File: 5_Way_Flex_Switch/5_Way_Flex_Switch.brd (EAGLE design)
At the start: 51 x 26.5 mm, 9 parts

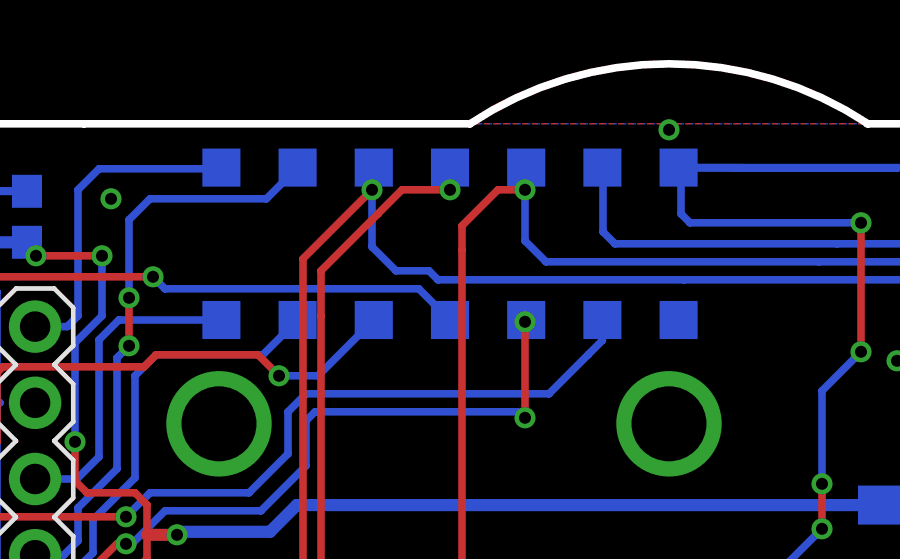
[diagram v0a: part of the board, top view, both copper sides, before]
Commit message: Updates/ label modifications to make them consistent
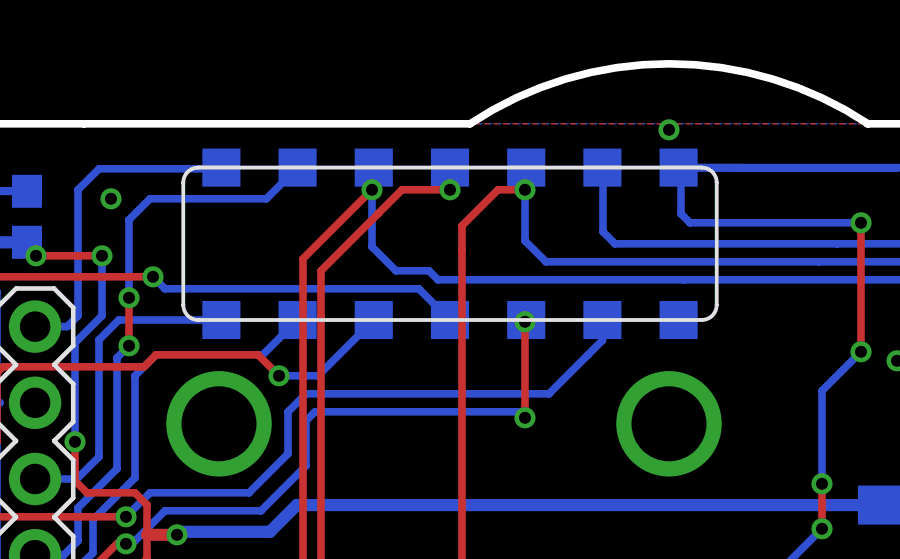
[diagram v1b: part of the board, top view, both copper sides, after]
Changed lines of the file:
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@@
 <contactref element="H2" pad="6"/>
 <contactref element="H2" pad="5"/>
+<wire x1="49.27" y1="13.52" x2="48" y2="21.7" width="0" layer="19" extent="1-1"/>
+<wire x1="46.73" y1="13.52" x2="49.27" y2="13.52" width="0" layer="19" extent="1-1"/>
+<wire x1="40.3" y1="14.5" x2="46.73" y2="13.52" width="0" layer="19" extent="1-1"/>
+<wire x1="42.5" y1="8" x2="40.3" y2="14.5" width="0" layer="19" extent="1-1"/>
+<wire x1="25.62" y1="17.96" x2="32.92" y2="16.62" width="0" layer="19" extent="16-16"/>
+<wire x1="25.3" y1="14.5" x2="25.62" y2="17.96" width="0" layer="19" extent="16-16"/>
+<wire x1="25.3" y1="24.3" x2="25.62" y2="17.96" width="0" layer="19" extent="16-16"/>
+<wire x1="20.6" y1="9.3" x2="25.3" y2="14.5" width="0" layer="19" extent="1-1"/>
+<wire x1="15.8" y1="9.3" x2="20.6" y2="9.3" width="0" layer="19" extent="1-1"/>
+<wire x1="12.4" y1="7.2" x2="15.8" y2="9.3" width="0" layer="19" extent="1-1"/>
+<wire x1="10.6" y1="9.3" x2="12.4" y2="7.2" width="0" layer="19" extent="1-1"/>
+<wire x1="10.3" y1="14.5" x2="10.6" y2="9.3" width="0" layer="19" extent="1-1"/>
+<wire x1="4.17" y1="15.2" x2="10.3" y2="14.5" width="0" layer="19" extent="1-1"/>
+<wire x1="3" y1="15.2" x2="4.17" y2="15.2" width="0" layer="19" extent="16-16"/>
+<wire x1="1.63" y1="15.2" x2="2.8" y2="15.2" width="0" layer="19" extent="16-16"/>
+<wire x1="4.17" y1="7.58" x2="2.92" y2="7.58" width="0" layer="19" extent="16-16"/>
+<wire x1="1.63" y1="7.58" x2="2.9" y2="7.6" width="0" layer="19" extent="16-16"/>
+<wire x1="6.7" y1="22" x2="3.9" y2="22.25" width="0" layer="19" extent="16-16"/>
+<wire x1="30" y1="7.9" x2="25.3" y2="14.5" width="0" layer="19" extent="1-1"/>
+<wire x1="33" y1="6.71" x2="30" y2="7.9" width="0" layer="19" extent="16-16"/>
+<wire x1="48.7" y1="2.2" x2="42.5" y2="8" width="0" layer="19" extent="1-1"/>
 </signal>
 <signal name="SW">
@@
 </signal>
 </signals>
-<errors>
-</errors>
 </board>
 </drawing>

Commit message: Licenses
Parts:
- removed MOD1: CONFIGURATION_BRD, CYCFI_Module_castellated:CONFIGURATION_BRD
- added CB1: (no value), CYCFI_Module_castellated:CONFIGURATION_BRD_PADS
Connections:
- removed net M1: MOD1.M1, U$1.M1
- removed net N2: MOD1.N2, U$1.N2
- new net N$13: CB1.M1, U$1.M1
- new net N$15: CB1.N2, U$1.N2
- new net N$16: CB1.M2, U$1.M2
- new net N$17: CB1.B2, U$1.B2
- new net N$2: CB1.COM2, U$1.COM2
- new net N$3: CB1.COM1, U$1.COM1
- net 1-IC: now also CB1.1-IC; no longer MOD1.1-IC
- net 1-OC: now also CB1.1-OC; no longer MOD1.1-OC
- net 2-IC: now also CB1.2-IC; no longer MOD1.2-IC
- net 2-OC: now also CB1.2-OC; no longer MOD1.2-OC
- net 3-IC: now also CB1.3-IC; no longer MOD1.3-IC
- net 3-OC: now also CB1.3-OC; no longer MOD1.3-OC
- net 4-IC: now also CB1.4-IC; no longer MOD1.4-IC
- net 4-OC: now also CB1.4-OC; no longer MOD1.4-OC
- net B1: now also CB1.B1; no longer MOD1.B1
- net GND: now also CB1.GND, CB1.GND1; no longer MOD1.GND
- net IN+: now also CB1.OUT-; no longer U$1.COM1
- net IN-: now also CB1.OUT+; no longer MOD1.IN-, U$1.COM2
- net N1: now also CB1.N1; no longer MOD1.N1
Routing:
- net GND: track 30.1 -> 102.5 mm, vias 14 -> 4
- net IN-: track 64.5 -> 15.1 mm, vias 4 -> 0
- net N$2: track 0.00 -> 46.4 mm, vias 0 -> 1
- net N$15: track 0.00 -> 44.5 mm, vias 0 -> 1
- net N$16: track 0.00 -> 43.5 mm, vias 0 -> 2
- net N2: track 39.6 -> 0.00 mm, vias 2 -> 0
- net N$13: track 0.00 -> 36.0 mm, vias 0 -> 1
- net GND1: track 0.00 -> 33.3 mm, vias 0 -> 2
- net N$17: track 0.00 -> 32.9 mm, vias 0 -> 4
- net M1: track 25.8 -> 0.00 mm, vias 1 -> 0
- net N$3: track 0.00 -> 25.3 mm, vias 0 -> 1
- net IN+: track 39.8 -> 15.7 mm
- net 4-OC: track 26.2 -> 41.1 mm, vias 1 -> 3
- net N1: track 63.8 -> 76.7 mm, vias 2 -> 4
- net VBATT: track 54.3 -> 65.3 mm, vias 4 -> 6
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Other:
- outline, holes or cut-outs redrawn
